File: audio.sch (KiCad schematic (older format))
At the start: 1 part, among them J3 Micro_SD_Card_Det

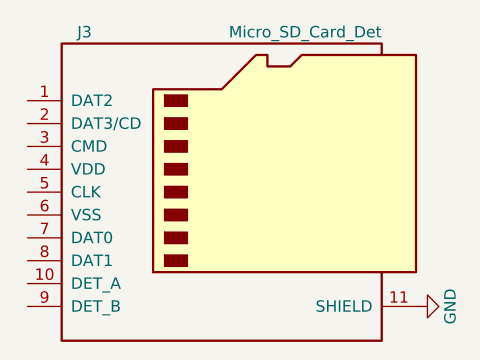
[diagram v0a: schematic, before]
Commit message: audio jack placed
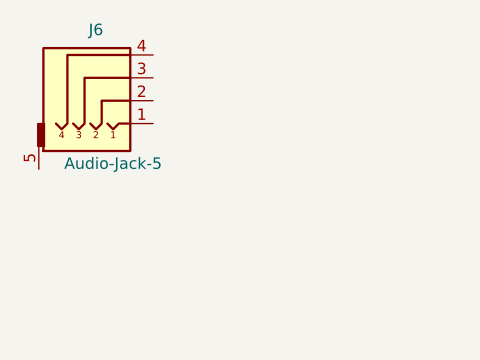
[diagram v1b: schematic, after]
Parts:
- removed J3: Micro_SD_Card_Det, micro-sd:SCHD3A100, symbol Micro_SD_Card_Det
- added J6: Audio-Jack-5, audio-jack:CUI_SJ-43516-SMT, symbol Audio-Jack-5
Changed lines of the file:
@@
 $Descr A4 11693 8268
 encoding utf-8
-Sheet 2 10
+Sheet 10 10
 Title ""
 Date ""
@@
 $EndDescr
 $Comp
-L Micro_SD_Card_Det J3
-U 1 1 5A12C57E
-P 4200 2950
-F 0 "J3" H 3550 3650 50  0000 C CNN
-F 1 "Micro_SD_Card_Det" H 4850 3650 50  0000 R CNN
-F 2 "micro-sd:SCHD3A100" H 6250 3650 50  0001 C CNN
-F 3 "http://www.mouser.com/ds/2/15/Alps_01172017_SCHD3A0100-1155838.pdf" H 4200 3050 50  0001 C CNN
-	1    4200 2950
+L Audio-Jack-5 J6
+U 1 1 5A133C61
+P 3650 2450
+F 0 "J6" H 3600 2660 50  0000 C CNN
+F 1 "Audio-Jack-5" H 3675 2075 50  0000 C CNN
+F 2 "audio-jack:CUI_SJ-43516-SMT" H 3900 2550 50  0001 C CNN
+F 3 "" H 3900 2550 50  0001 C CNN
+	1    3650 2450
 	1    0    0    -1
 $EndComp
-$Comp
-L GND #PWR1
-U 1 1 5A12C74D
-P 5000 3450
-F 0 "#PWR1" H 5000 3200 50  0001 C CNN
-F 1 "GND" H 5000 3300 50  0000 C CNN
-F 2 "" H 5000 3450 50  0001 C CNN
-F 3 "" H 5000 3450 50  0001 C CNN
-	1    5000 3450
-	0    -1   -1   0
-$EndComp
 $EndSCHEMATC
